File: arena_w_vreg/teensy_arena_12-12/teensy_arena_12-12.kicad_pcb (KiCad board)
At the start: 4 copper layers, 254 x 254 mm, 87 parts, among them J1 Barrel_Jack, J2 Conn_01x04, J3 Conn_01x04, P1 CONN15, P10 CONN15, P11 CONN15, P12 CONN15, P2 CONN15, P3 CONN15, P4 CONN15, P5 CONN15, P6 CONN15, P7 CONN15, P8 CONN15, P9 CONN15, Q2 MOSFET_NCHAN, SW1 SW_SPDT, U1 TXB0108PW, U10 AZ1084-5.0, U11 AZ1084-5.0, U12 AZ1084-5.0, U13 AZ1084-5.0, U14 AZ1084-5.0, U15 AZ1084-5.0, U16 AZ1084-5.0, U17 AZ1084-5.0, U18 Teensy4.1, U2 TXB0108PW, U3 TXB0108PW, U4 TXB0108PW, U5 TXB0108PW, U6 AZ1084-5.0, U7 AZ1084-5.0, U8 AZ1084-5.0, U9 AZ1084-5.0

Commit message: Added new pcb routing for 12-12 with vreg.
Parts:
- J2, J3: footprint Connector_JST:JST_SH_SM04B-SRSS-TB_1x04-1MP_P1.00mm_Horizontal -> arena_custom:JST_SH_SM04B-SRSS-TB_1x04-1MP_P1.00mm_Horizontal
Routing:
- net /Panel Headers/RESET: track 0.00 -> 573.1 mm, vias 0 -> 3
- net /Level Shifters/PAN5V.EXT_INT: track 0.00 -> 572.9 mm, vias 0 -> 4
- net /Level Shifters/PAN5V.CS_16: track 0.00 -> 485.8 mm, vias 0 -> 4
- net /Level Shifters/PAN5V.CS_18: track 0.00 -> 385.3 mm, vias 0 -> 2
- net /Level Shifters/PAN5V.CS_17: track 0.00 -> 383.2 mm, vias 0 -> 2
- net /Level Shifters/PAN5V.CS_19: track 0.00 -> 383.0 mm, vias 0 -> 3
- net /Level Shifters/PAN5V.CS_09: track 0.00 -> 366.2 mm, vias 0 -> 3
- net /Level Shifters/PAN5V.CS_27: track 0.00 -> 363.5 mm, vias 0 -> 2
- net /Level Shifters/PAN5V.CS_25: track 0.00 -> 359.5 mm, vias 0 -> 3
- net /Level Shifters/PAN5V.CS_28: track 0.00 -> 356.2 mm, vias 0 -> 2
- net /Level Shifters/PAN5V.CS_08: track 0.00 -> 355.8 mm, vias 0 -> 2
- net /Level Shifters/PAN5V.CS_15: track 0.00 -> 353.9 mm, vias 0 -> 3
- net /Level Shifters/PAN5V.CS_13: track 0.00 -> 350.9 mm, vias 0 -> 2
- net /Level Shifters/PAN5V.CS_14: track 0.00 -> 349.6 mm, vias 0 -> 4
- net /Level Shifters/PAN5V.CS_02: track 0.00 -> 347.3 mm, vias 0 -> 1
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
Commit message: Worked on routing 12-12 arean with vreg.
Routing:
- net /Panel Headers/RESET: track 573.1 -> 579.9 mm
- net /Level Shifters/PAN5V.SCK_0: track 288.7 -> 292.2 mm
- net /Level Shifters/PAN5V.CS_02: track 347.3 -> 349.8 mm
- net /Level Shifters/PAN5V.MOSI_0: track 296.9 -> 299.3 mm
- net /Level Shifters/PAN5V.SCK_1: track 290.5 -> 292.7 mm
- net /Level Shifters/PAN5V.CS_16: track 485.8 -> 483.7 mm
- net /Level Shifters/PAN5V.MOSI_1: track 285.3 -> 287.1 mm
- net /Level Shifters/PAN5V.EXT_INT: track 572.9 -> 574.6 mm
- net /Level Shifters/PAN5V.CS_01: track 344.8 -> 346.4 mm
- net /Level Shifters/PAN5V.MISO_0: track 297.5 -> 299.0 mm
- net /Level Shifters/PAN5V.CS_24: track 338.2 -> 339.6 mm
- net /Level Shifters/PAN5V.CS_28: track 356.2 -> 357.6 mm
- net /Level Shifters/PAN5V.CS_00: track 308.7 -> 307.4 mm
- net /Level Shifters/PAN5V.CS_26: track 342.4 -> 343.6 mm
- net /Level Shifters/PAN5V.CS_20: track 338.7 -> 339.8 mm
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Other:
- outline, holes or cut-outs redrawn

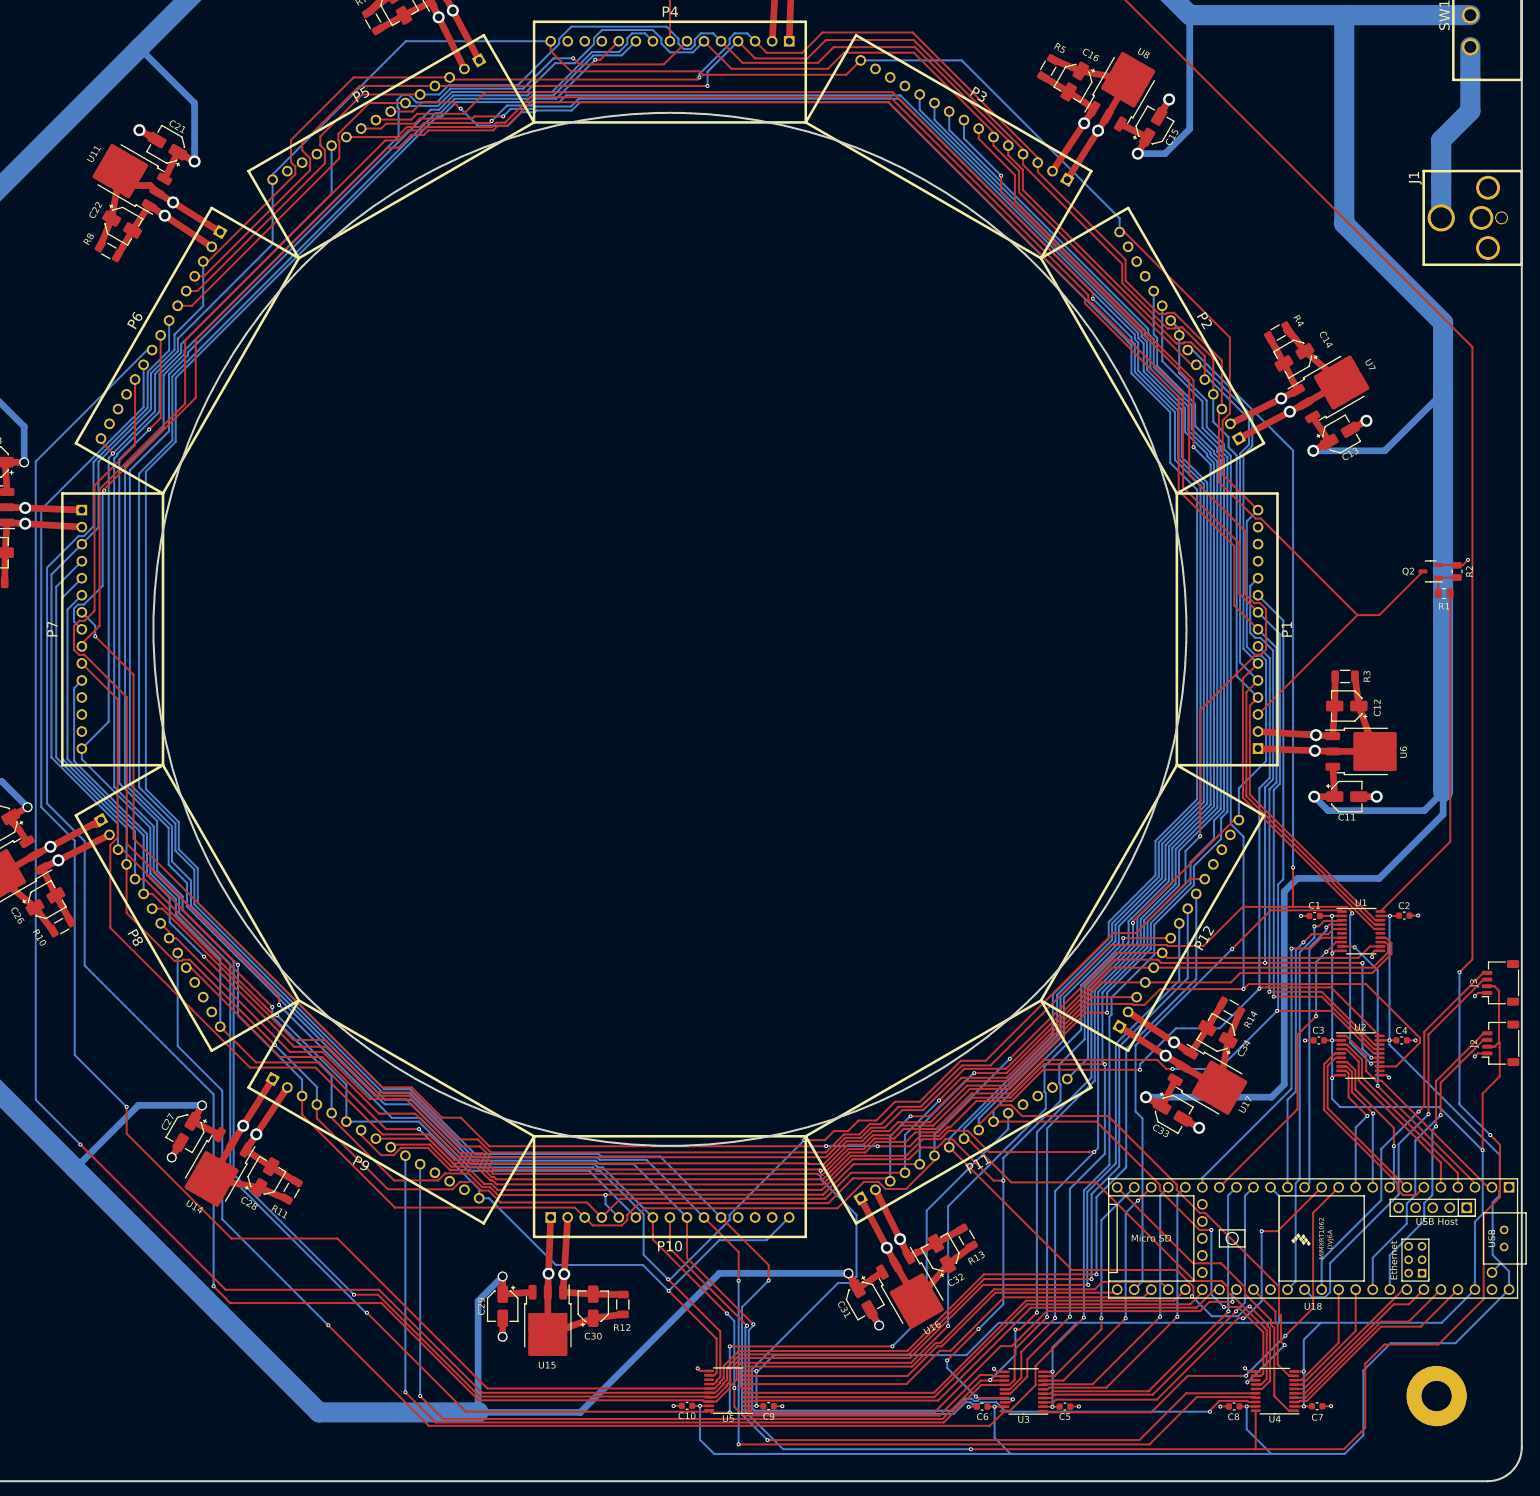
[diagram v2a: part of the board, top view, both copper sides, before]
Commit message: More work on routing.
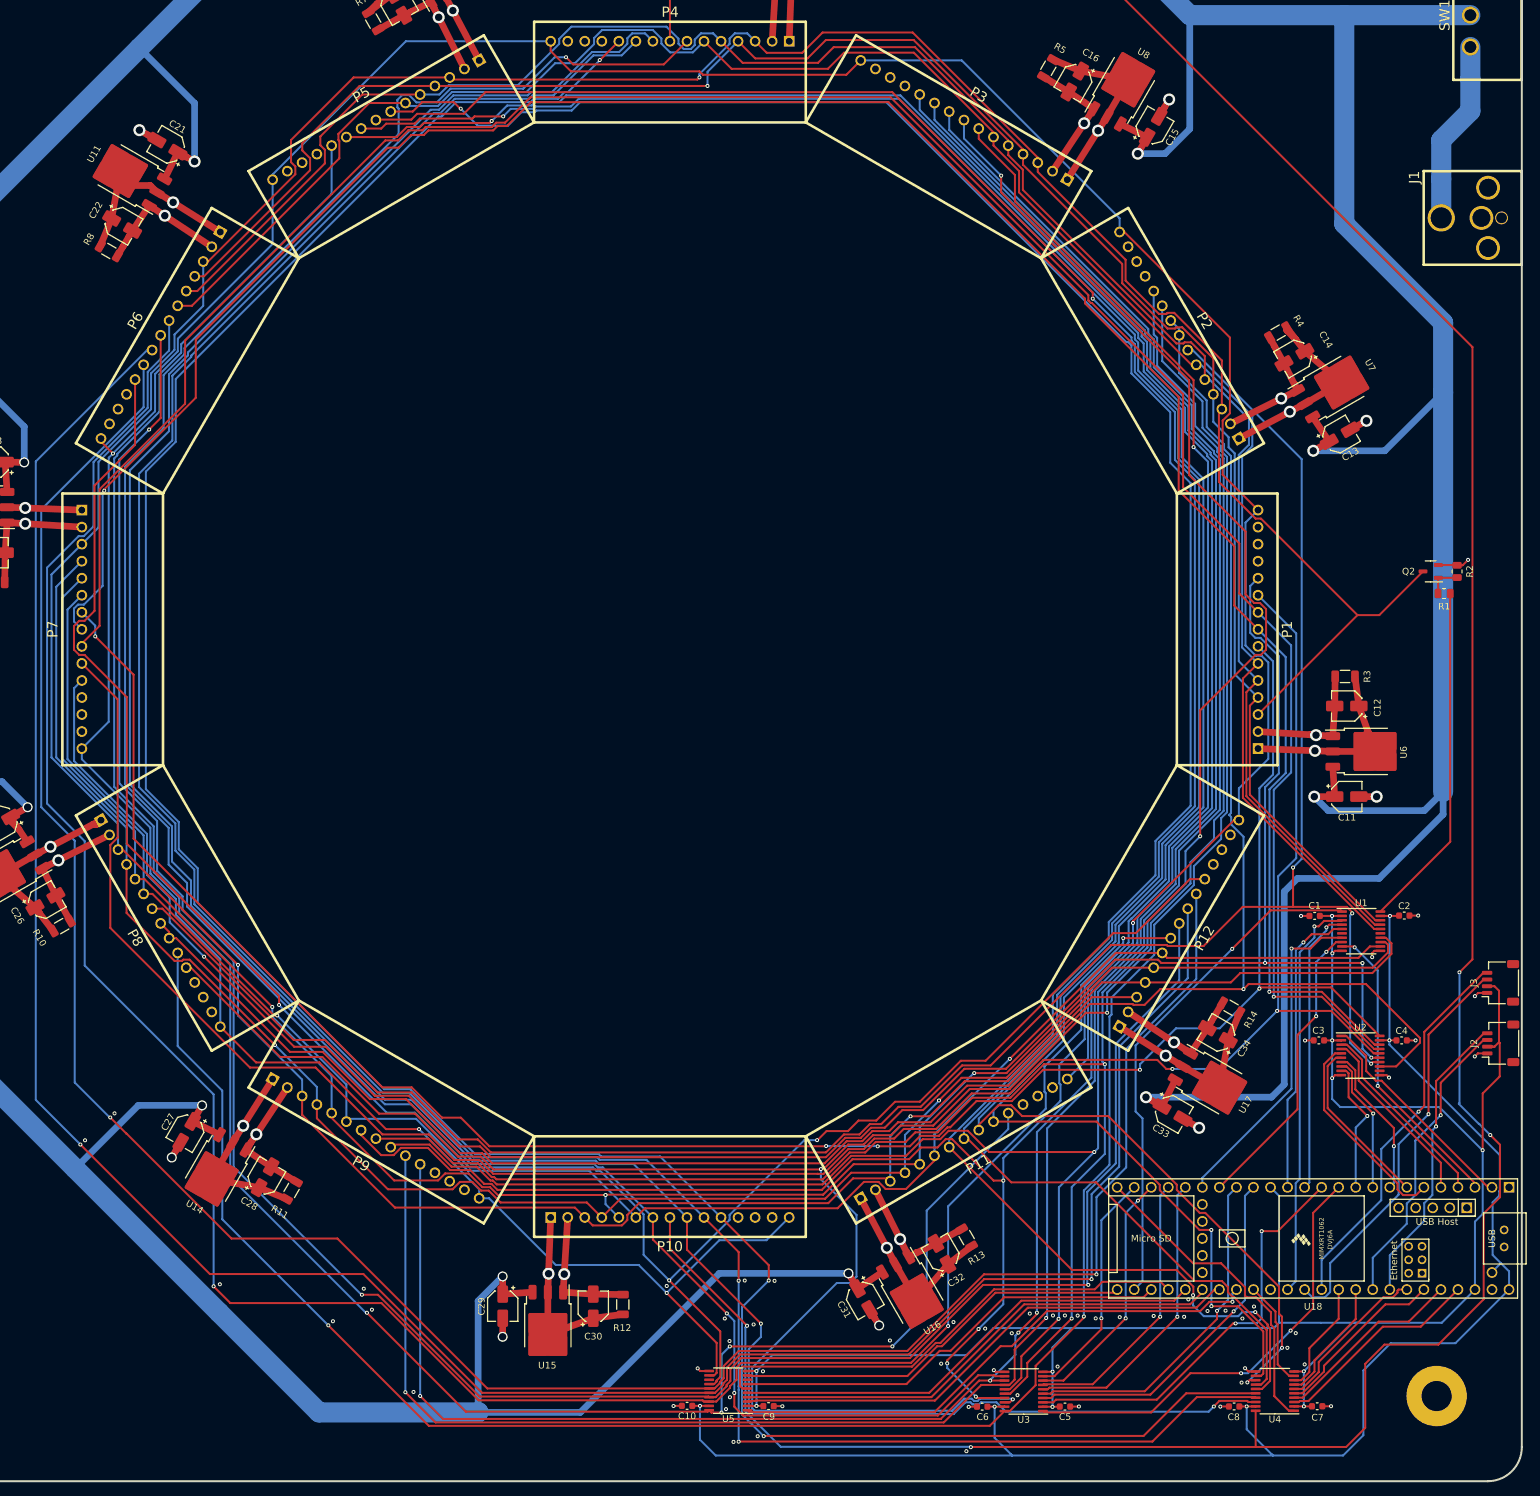
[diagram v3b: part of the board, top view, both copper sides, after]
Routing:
- net +3.3V: track 289.8 -> 291.5 mm
- net /Level Shifters/PAN3V.CS_09: track 61.0 -> 62.4 mm
- net /Level Shifters/PAN5V.CS_03: track 324.4 -> 325.8 mm
- net /Level Shifters/PAN5V.CS_02: track 349.8 -> 351.2 mm
- net /Level Shifters/PAN5V.CS_01: track 346.4 -> 347.5 mm
- net /Level Shifters/PAN5V.CS_05: track 324.9 -> 326.0 mm
- net /Level Shifters/PAN3V.CS_20: track 22.9 -> 24.0 mm
- net /Level Shifters/PAN5V.CS_20: track 339.8 -> 338.9 mm
- net /Level Shifters/PAN5V.CS_22: track 345.2 -> 344.3 mm
- net +5V: track 237.8 -> 238.7 mm
- net /Level Shifters/PAN5V.CS_17: track 384.3 -> 385.1 mm
- net /Level Shifters/PAN3V.CS_16: track 47.1 -> 47.9 mm
- net /Level Shifters/PAN5V.CS_24: track 339.6 -> 338.9 mm
- net /Level Shifters/PAN5V.CS_04: track 323.3 -> 324.0 mm
- net /Level Shifters/PAN5V.CS_21: track 335.1 -> 334.4 mm
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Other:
- outline, holes or cut-outs redrawn

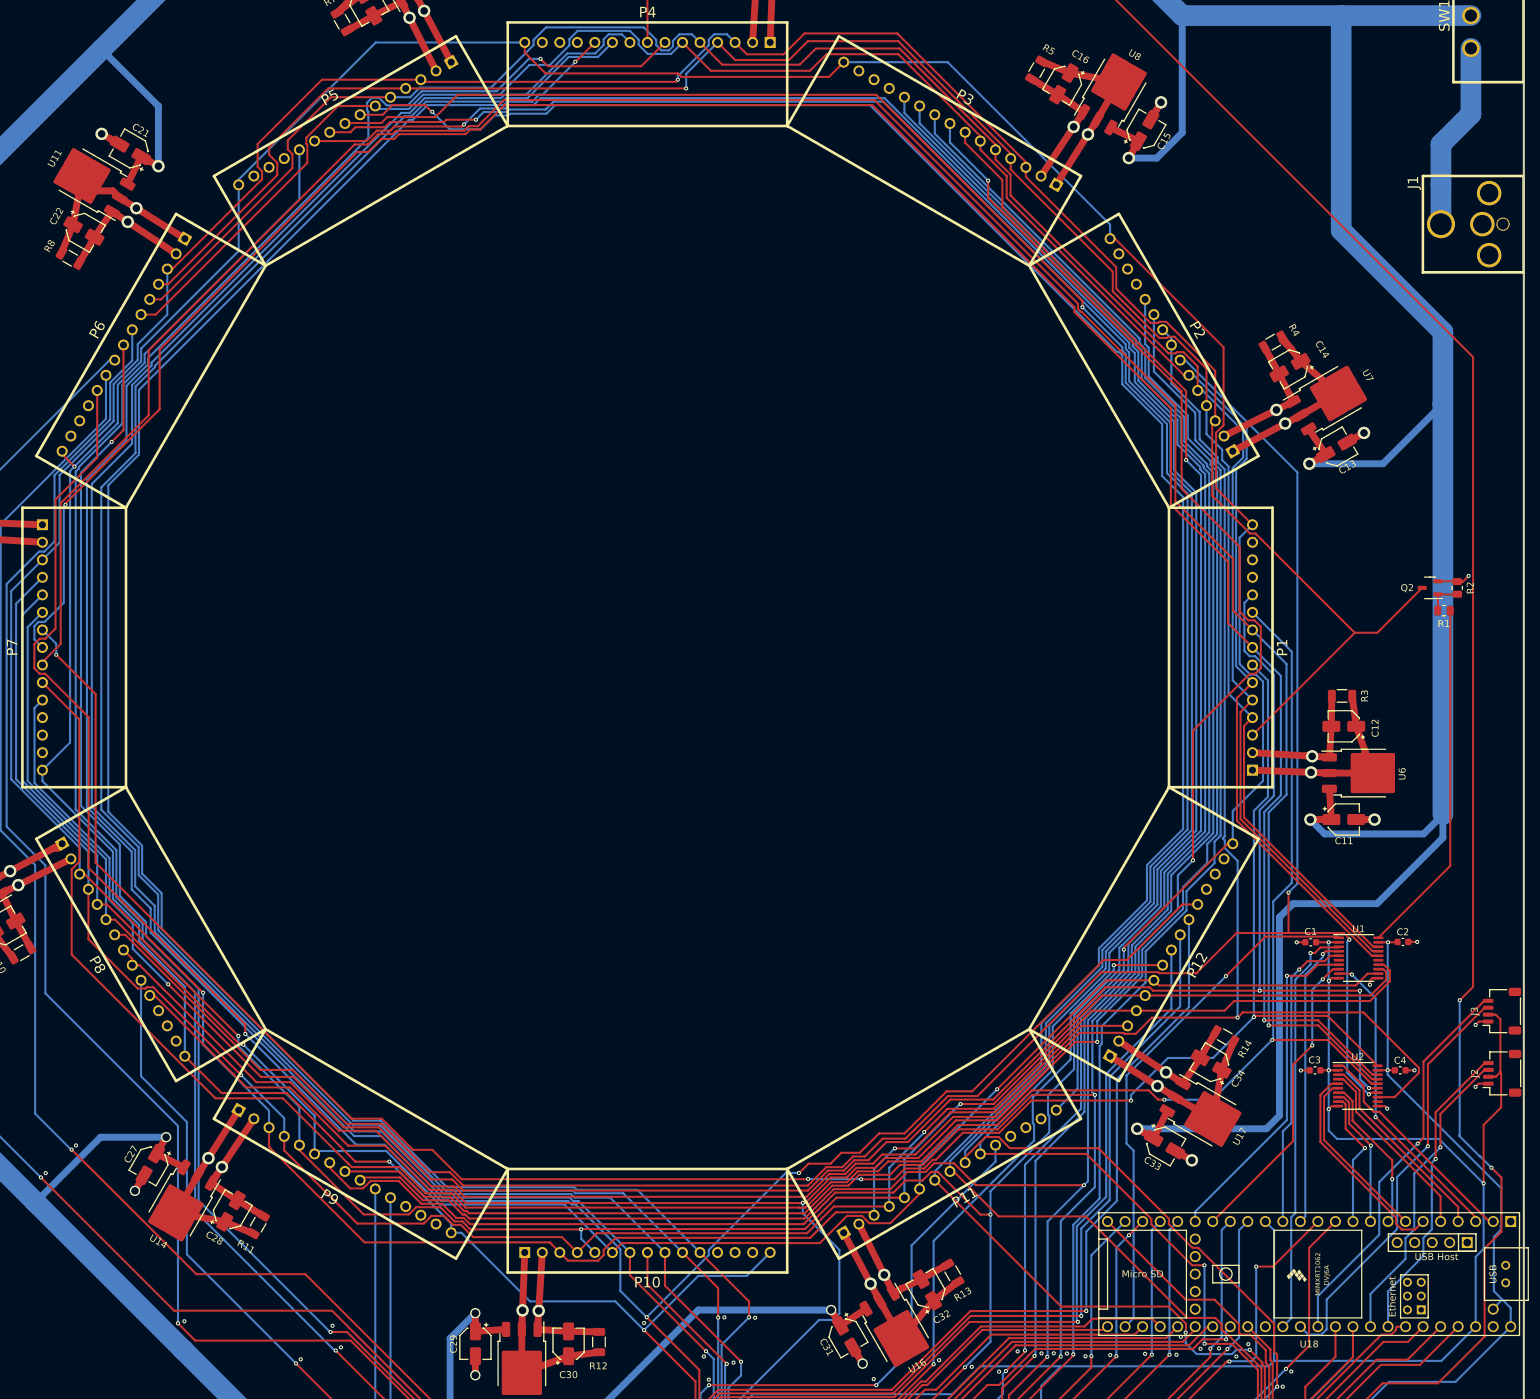
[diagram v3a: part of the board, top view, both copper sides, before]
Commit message: More work on routing of 12-12 arean with vreg.
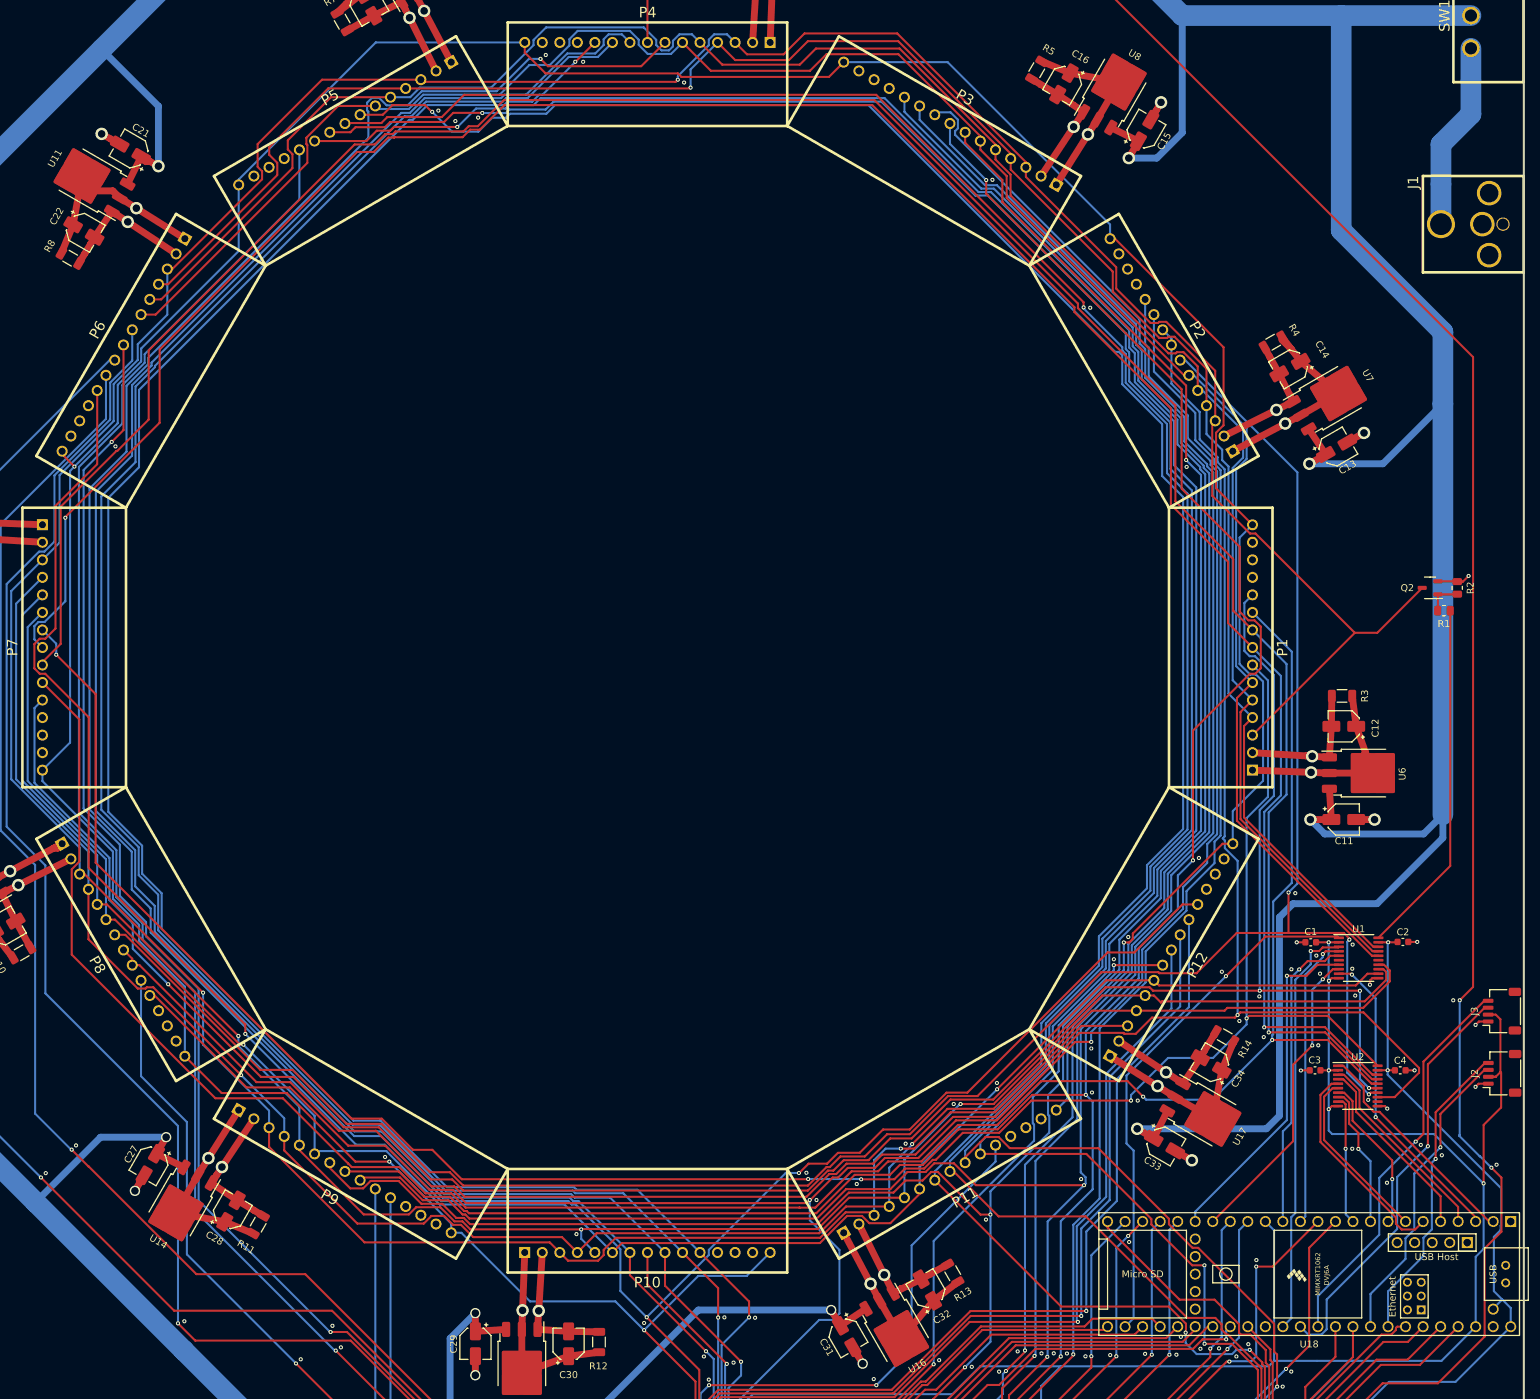
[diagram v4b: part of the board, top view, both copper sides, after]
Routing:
- net /Level Shifters/PAN5V.CS_12: track 333.1 -> 335.9 mm
- net /Level Shifters/PAN3V.CS_07: track 20.1 -> 18.7 mm
- net /Level Shifters/PAN5V.CS_00: track 307.8 -> 308.9 mm
- net /Level Shifters/PAN5V.CS_03: track 325.8 -> 326.9 mm
- net /Level Shifters/PAN5V.CS_14: track 348.9 -> 350.0 mm
- net /Level Shifters/PAN5V.CS_23: track 337.7 -> 338.7 mm
- net /Level Shifters/PAN5V.CS_13: track 350.7 -> 351.8 mm
- net /Level Shifters/PAN5V.CS_22: track 344.3 -> 345.3 mm
- net /Level Shifters/PAN5V.EXT_INT: track 575.1 -> 576.0 mm
- net /Level Shifters/PAN5V.MOSI_1: track 287.1 -> 287.9 mm
- net /Level Shifters/PAN5V.CS_11: track 344.7 -> 344.0 mm
- net /Panel Headers/RESET: track 579.9 -> 580.7 mm
- net /Level Shifters/PAN5V.CS_01: track 347.5 -> 348.1 mm
- net /Level Shifters/PAN5V.CS_02: track 351.2 -> 351.7 mm
- net /Level Shifters/PAN3V.CS_16: track 47.9 -> 48.4 mm
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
